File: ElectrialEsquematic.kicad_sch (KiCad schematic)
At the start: 12 parts, among them U2 ESP32_NODEMCU, U3 TP4056

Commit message: Fix some lines
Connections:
- net at 100n.2, 10n.2, 5V.2 (-)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: now also LoRa.1 (GND), LoRa.10 (GND), LoRa.8 (GND)
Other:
- moved on the sheet: LCD
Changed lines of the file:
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@@
   (junction (at 129.54 125.73) (diameter 0) (color 0 0 0 0)
   )
+  (junction (at 76.2 125.73) (diameter 0) (color 0 0 0 0)
+  )
   (junction (at 129.54 118.11) (diameter 0) (color 0 0 0 0)
   )
-  (wire (pts (xy 139.7 97.79) (xy 153.67 99.06))
+  (junction (at 124.46 125.73) (diameter 0) (color 0 0 0 0)
+  )
+  (wire (pts (xy 139.7 97.79) (xy 156.21 97.79))
     (stroke (width 0) (type default) (color 0 0 0 0))
   )
@@
     (stroke (width 0) (type default) (color 0 0 0 0))
   )
+  (wire (pts (xy 124.46 125.73) (xy 129.54 125.73))
+    (stroke (width 0) (type default) (color 0 0 0 0))
+  )
   (wire (pts (xy 167.64 90.17) (xy 151.13 90.17))
     (stroke (width 0) (type default) (color 0 0 0 0))
@@
     (stroke (width 0) (type default) (color 0 0 0 0))
   )
-  (wire (pts (xy 76.2 125.73) (xy 129.54 125.73))
+  (wire (pts (xy 59.69 125.73) (xy 76.2 125.73))
     (stroke (width 0) (type default) (color 0 0 0 0))
   )
@@
     (stroke (width 0) (type default) (color 0 0 0 0))
   )
+  (wire (pts (xy 76.2 125.73) (xy 124.46 125.73))
+    (stroke (width 0) (type default) (color 0 0 0 0))
+  )
   (wire (pts (xy 48.26 78.74) (xy 48.26 81.28))
     (stroke (width 0) (type default) (color 0 0 0 0))
   )
-  (wire (pts (xy 143.51 111.76) (xy 137.16 110.49))
+  (wire (pts (xy 146.05 110.49) (xy 137.16 110.49))
     (stroke (width 0) (type default) (color 0 0 0 0))
   )
@@
     (stroke (width 0) (type default) (color 0 0 0 0))
   )
-  (wire (pts (xy 143.51 109.22) (xy 138.43 107.95))
+  (wire (pts (xy 146.05 107.95) (xy 138.43 107.95))
     (stroke (width 0) (type default) (color 0 0 0 0))
   )
@@
     (stroke (width 0) (type default) (color 0 0 0 0))
   )
+  (wire (pts (xy 124.46 125.73) (xy 124.46 119.38))
+    (stroke (width 0) (type default) (color 0 0 0 0))
+  )
   (wire (pts (xy 137.16 87.63) (xy 137.16 62.23))
     (stroke (width 0) (type default) (color 0 0 0 0))
@@
     (stroke (width 0) (type default) (color 0 0 0 0))
   )
-  (wire (pts (xy 153.67 124.46) (xy 153.67 127))
+  (wire (pts (xy 156.21 123.19) (xy 153.67 127))
     (stroke (width 0) (type default) (color 0 0 0 0))
   )
@@
     (pin "2")
   )
-  (symbol (lib_id "Display_Character:NHD-C0220BIZ") (at 153.67 111.76 0) (unit 1)
-    (in_bom yes) (on_board yes) (fields_autoplaced)
-    (property "Reference" "LCD" (id 0) (at 155.6894 96.52 0)
-      (effects (font (size 1.27 1.27)) (justify left))
-    )
-    (property "Value" "NHD-C0220BIZ" (id 1) (at 155.6894 99.06 0)
-      (effects (font (size 1.27 1.27)) (justify left))
-    )
-    (property "Footprint" "Display:NHD-C0220BiZ" (id 2) (at 153.67 127 0)
-      (effects (font (size 1.27 1.27)) hide)
-    )
-    (property "Datasheet" "http://www.newhavendisplay.com/specs/NHD-C0220BiZ-FSW-FBW-3V3M.pdf" (id 3) (at 146.05 96.52 0)
-      (effects (font (size 1.27 1.27)) hide)
-    )
+  (symbol (lib_id "Display_Character:NHD-C0220BIZ") (at 156.21 110.49 0) (unit 1)
+    (in_bom yes) (on_board yes) (fields_autoplaced)
+    (property "Reference" "LCD" (id 0) (at 158.2294 95.25 0)
+      (effects (font (size 1.27 1.27)) (justify left))
+    )
+    (property "Value" "NHD-C0220BIZ" (id 1) (at 158.2294 97.79 0)
+      (effects (font (size 1.27 1.27)) (justify left))
+    )
+    (property "Footprint" "Display:NHD-C0220BiZ" (id 2) (at 156.21 125.73 0)
+      (effects (font (size 1.27 1.27)) hide)
+    )
+    (property "Datasheet" "http://www.newhavendisplay.com/specs/NHD-C0220BiZ-FSW-FBW-3V3M.pdf" (id 3) (at 148.59 95.25 0)
+      (effects (font (size 1.27 1.27)) hide)
+    )

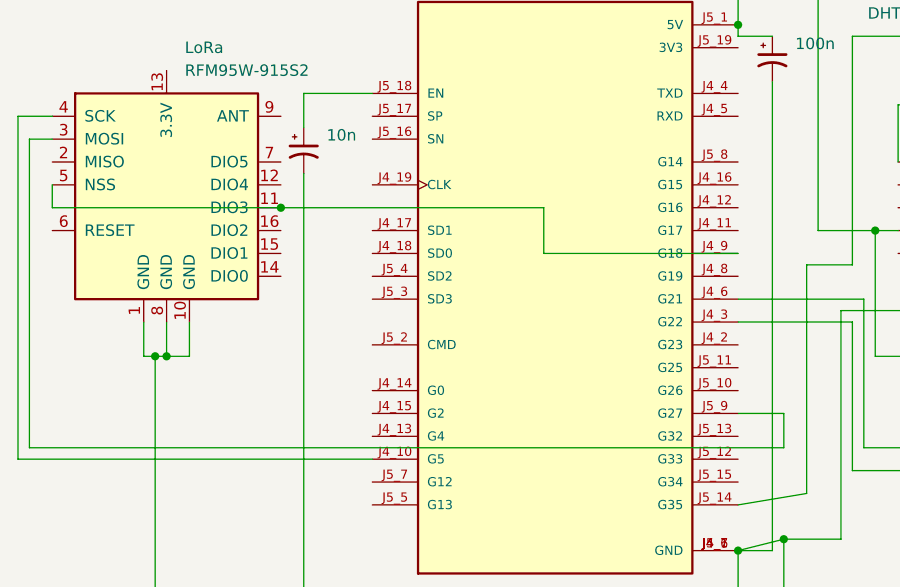
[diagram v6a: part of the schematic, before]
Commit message: Add MISO at Lora
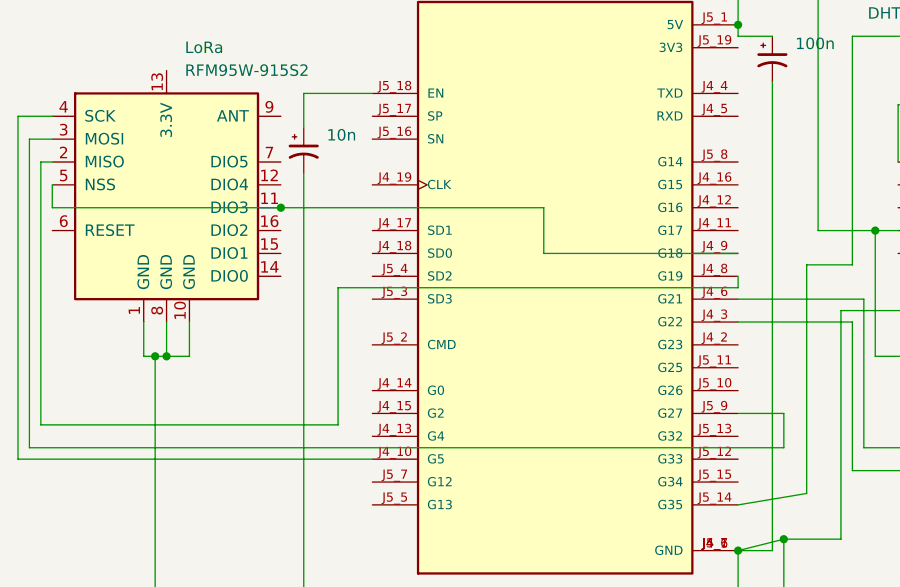
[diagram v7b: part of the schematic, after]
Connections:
- net at LoRa.2 (MISO): now also U2.J4_8 (G19)
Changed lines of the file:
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@@
+    (stroke (width 0) (type default) (color 0 0 0 0))
+  )
+  (wire (pts (xy 46.99 76.2) (xy 48.26 76.2))
     (stroke (width 0) (type default) (color 0 0 0 0))
   )
@@
   )
   (wire (pts (xy 151.13 50.8) (xy 133.35 50.8))
+    (stroke (width 0) (type default) (color 0 0 0 0))
+  )
+  (wire (pts (xy 80.01 105.41) (xy 46.99 105.41))
     (stroke (width 0) (type default) (color 0 0 0 0))
   )
@@
     (stroke (width 0) (type default) (color 0 0 0 0))
   )
+  (wire (pts (xy 80.01 90.17) (xy 80.01 105.41))
+    (stroke (width 0) (type default) (color 0 0 0 0))
+  )
   (wire (pts (xy 137.16 62.23) (xy 158.75 62.23))
     (stroke (width 0) (type default) (color 0 0 0 0))
@@
   )
   (wire (pts (xy 73.66 81.28) (xy 48.26 81.28))
+    (stroke (width 0) (type default) (color 0 0 0 0))
+  )
+  (wire (pts (xy 124.46 88.9) (xy 124.46 90.17))
     (stroke (width 0) (type default) (color 0 0 0 0))
   )
@@
     (stroke (width 0) (type default) (color 0 0 0 0))
   )
+  (wire (pts (xy 124.46 90.17) (xy 80.01 90.17))
+    (stroke (width 0) (type default) (color 0 0 0 0))
+  )
   (wire (pts (xy 137.16 110.49) (xy 137.16 93.98))
     (stroke (width 0) (type default) (color 0 0 0 0))
@@
     (stroke (width 0) (type default) (color 0 0 0 0))
   )
+  (wire (pts (xy 46.99 105.41) (xy 46.99 76.2))
+    (stroke (width 0) (type default) (color 0 0 0 0))
+  )
